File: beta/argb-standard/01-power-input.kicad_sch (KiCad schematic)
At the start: 9 parts, among them J1 SATA_PWR_15P, Q1 AO4407A

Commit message: Audit BETA electrical and pour pipeline
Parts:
- RT1: MPN MF72-5D-20 -> MF72 5D20
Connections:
- net at Q1.1 (S), Q1.2 (S), Q1.3 (S): now also F1.1; no longer J1.7 (Pin_7), J1.8 (Pin_8), J1.9 (Pin_9)
- net at Q1.5 (D), Q1.6 (D), Q1.7 (D)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: now also J1.7 (Pin_7), J1.8 (Pin_8), J1.9 (Pin_9); no longer F1.1
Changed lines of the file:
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@@
 	(symbol
 		(lib_id "cec-vendor:AO4407A")
-		(at 153.67 123.19 270)
-		(unit 1)
-		(exclude_from_sim no)
-		(in_bom yes)
-		(on_board yes)
-		(dnp no)
-		(fields_autoplaced yes)
-		(property "Reference" "Q1" (at 153.67 101.6 90) (effects (font (size 1.27 1.27))))
-		(property "Value" "AO4407A" (at 153.67 130.81 90) (effects (font (size 1.27 1.27))))
+		(at 153.67 123.19 90)
+		(unit 1)
+		(exclude_from_sim no)
+		(in_bom yes)
+		(on_board yes)
+		(dnp no)
+		(fields_autoplaced yes)
+		(property "Reference" "Q1" (at 153.67 106.68 90) (effects (font (size 1.27 1.27))))
+		(property "Value" "AO4407A" (at 153.67 101.6 90) (effects (font (size 1.27 1.27))))
 		(property "Footprint" "cec-Package_SO:SOIC-8_L4.9-W3.9-P1.27-LS6.0-BL" (at 153.67 123.19 0) (effects (font (size 1.27 1.27)) (hide yes)))
-		(property "Datasheet" "" (at 153.67 123.19 0) (effects (font (size 1.27 1.27)) (hide yes)))
+		(property "Datasheet" "https://www.aosmd.com/res/datasheets/AO4407A.pdf" (at 153.67 123.19 0) (effects (font (size 1.27 1.27)) (hide yes)))
 		(property "Manufacturer" "Alpha & Omega Semiconductor" (at 153.67 123.19 0) (effects (font (size 1.27 1.27)) (hide yes)))
 		(property "MPN" "AO4407A" (at 153.67 123.19 0) (effects (font (size 1.27 1.27)) (hide yes)))
@@
 		(property "Value" "2920L700/12MR" (at 185.42 118.36 0) (effects (font (size 1.27 1.27))))
 		(property "Footprint" "cec-Fuse_SMD:F2920" (at 185.42 123.19 0) (effects (font (size 1.27 1.27)) (hide yes)))
-		(property "Datasheet" "" (at 185.42 123.19 0) (effects (font (size 1.27 1.27)) (hide yes)))
+		(property "Datasheet" "https://www.lcsc.com/datasheet/C207092.pdf" (at 185.42 123.19 0) (effects (font (size 1.27 1.27)) (hide yes)))
 		(property "Manufacturer" "Littelfuse" (at 185.42 123.19 0) (effects (font (size 1.27 1.27)) (hide yes)))
 		(property "MPN" "2920L700/12MR" (at 185.42 123.19 0) (effects (font (size 1.27 1.27)) (hide yes)))
@@
 		(property "Value" "MF72-5D-20" (at 210.82 118.36 0) (effects (font (size 1.27 1.27))))
 		(property "Footprint" "cec-Thermistor_THT:RES-TH_L22.0-W7.0-P10.00-D1.0-S2.00" (at 210.82 123.19 0) (effects (font (size 1.27 1.27)) (hide yes)))
-		(property "Datasheet" "" (at 210.82 123.19 0) (effects (font (size 1.27 1.27)) (hide yes)))
+		(property "Datasheet" "https://www.lcsc.com/datasheet/C122780.pdf" (at 210.82 123.19 0) (effects (font (size 1.27 1.27)) (hide yes)))
 		(property "Manufacturer" "Nanjing Shiheng Electronics" (at 210.82 123.19 0) (effects (font (size 1.27 1.27)) (hide yes)))
-		(property "MPN" "MF72-5D-20" (at 210.82 123.19 0) (effects (font (size 1.27 1.27)) (hide yes)))
+		(property "MPN" "MF72 5D20" (at 210.82 123.19 0) (effects (font (size 1.27 1.27)) (hide yes)))
 		(property "LCSC" "C122780" (at 210.82 123.19 0) (effects (font (size 1.27 1.27)) (hide yes)))
 		(property "Description" "Power NTC inrush-current limiter, 5 ohm cold / 7A rated (controlled inrush element -- spec Sec 7.2; OOS at LCSC as of 2026-07-05, flagged, matches this repo's own precedent for a real-but-thin-stock part, cf. the ESP32-S3-MINI-1 pick below)" (at 210.82 123.19 0) (effects (font (size 1.27 1.27)) (hide yes)))
@@
 	(symbol
 		(lib_id "cec-vendor:R_Small")
-		(at 153.67 100.33 0)
-		(unit 1)
-		(exclude_from_sim no)
-		(in_bom yes)
-		(on_board yes)
-		(dnp no)
-		(fields_autoplaced yes)
-		(property "Reference" "R1" (at 155.702 99.06 0) (effects (font (size 1.27 1.27)) (justify left)))
-		(property "Value" "10kΩ" (at 155.702 101.6 0) (effects (font (size 1.27 1.27)) (justify left)))
-		(property "Footprint" "cec-Resistor_SMD:R_0402_1005Metric" (at 153.67 100.33 0) (effects (font (size 1.27 1.27)) (hide yes)))
-		(property "Datasheet" "" (at 153.67 100.33 0) (effects (font (size 1.27 1.27)) (hide yes)))
-		(property "Manufacturer" "UNI-ROYAL" (at 153.67 100.33 0) (effects (font (size 1.27 1.27)) (hide yes)))
-		(property "MPN" "0402WGF1002TCE" (at 153.67 100.33 0) (effects (font (size 1.27 1.27)) (hide yes)))
-		(property "LCSC" "C25744" (at 153.67 100.33 0) (effects (font (size 1.27 1.27)) (hide yes)))
+		(at 153.67 115.57 0)
+		(unit 1)
+		(exclude_from_sim no)
+		(in_bom yes)
+		(on_board yes)
+		(dnp no)
+		(fields_autoplaced yes)
+		(property "Reference" "R1" (at 156.972 114.3 0) (effects (font (size 1.27 1.27)) (justify left)))
+		(property "Value" "10kΩ" (at 155.702 116.84 0) (effects (font (size 1.27 1.27)) (justify left)))
+		(property "Footprint" "cec-Resistor_SMD:R_0402_1005Metric" (at 153.67 115.57 0) (effects (font (size 1.27 1.27)) (hide yes)))
+		(property "Datasheet" "" (at 153.67 115.57 0) (effects (font (size 1.27 1.27)) (hide yes)))
+		(property "Manufacturer" "UNI-ROYAL" (at 153.67 115.57 0) (effects (font (size 1.27 1.27)) (hide yes)))
+		(property "MPN" "0402WGF1002TCE" (at 153.67 115.57 0) (effects (font (size 1.27 1.27)) (hide yes)))
+		(property "LCSC" "C25744" (at 153.67 115.57 0) (effects (font (size 1.27 1.27)) (hide yes)))
 		(pin "1")
 		(pin "2")
@@
 	(wire (pts (xy 135.89 123.19) (xy 146.05 123.19))
 		(stroke (width 0) (type default)))
+	(wire (pts (xy 135.89 120.65) (xy 146.05 120.65))
+		(stroke (width 0) (type default)))
+	(wire (pts (xy 135.89 125.73) (xy 146.05 125.73))
+		(stroke (width 0) (type default)))
+	(wire (pts (xy 135.89 118.11) (xy 146.05 118.11))
+		(stroke (width 0) (type default)))
+	(wire (pts (xy 135.89 118.11) (xy 135.89 120.65))
+		(stroke (width 0) (type default)))
+	(wire (pts (xy 135.89 120.65) (xy 135.89 123.19))
+		(stroke (width 0) (type default)))
 	(wire (pts (xy 135.89 123.19) (xy 135.89 125.73))
 		(stroke (width 0) (type default)))
-	(wire (pts (xy 135.89 125.73) (xy 146.05 125.73))
-		(stroke (width 0) (type default)))
-	(wire (pts (xy 135.89 123.19) (xy 135.89 120.65))
-		(stroke (width 0) (type default)))
-	(wire (pts (xy 135.89 120.65) (xy 146.05 120.65))
-		(stroke (width 0) (type default)))
 	(wire (pts (xy 161.29 123.19) (xy 171.45 123.19))
 		(stroke (width 0) (type default)))
+	(wire (pts (xy 161.29 120.65) (xy 171.45 120.65))
+		(stroke (width 0) (type default)))
 	(wire (pts (xy 161.29 125.73) (xy 171.45 125.73))
 		(stroke (width 0) (type default)))
-	(wire (pts (xy 161.29 120.65) (xy 171.45 120.65))
-		(stroke (width 0) (type default)))
-	(wire (pts (xy 161.29 128.27) (xy 171.45 128.27))
-		(stroke (width 0) (type default)))
-	(wire (pts (xy 171.45 120.65) (xy 171.45 128.27))
-		(stroke (width 0) (type default)))
-	(wire (pts (xy 153.67 115.57) (xy 153.67 102.87))
-		(stroke (width 0) (type default)))
-	(wire (pts (xy 171.45 125.73) (xy 171.45 123.19))
+	(wire (pts (xy 153.67 130.81) (xy 153.67 118.11))
 		(stroke (width 0) (type default)))
 	(wire (pts (xy 171.45 123.19) (xy 180.34 123.19))
 		(stroke (width 0) (type default)))
+	(wire (pts (xy 171.45 120.65) (xy 171.45 123.19))
+		(stroke (width 0) (type default)))
+	(wire (pts (xy 171.45 123.19) (xy 171.45 125.73))
+		(stroke (width 0) (type default)))
 	(wire (pts (xy 190.5 123.19) (xy 205.74 123.19))
 		(stroke (width 0) (type default)))
@@
 	(wire (pts (xy 110.49 133.35) (xy 104.14 133.35))
 		(stroke (width 0) (type default)))
-	(wire (pts (xy 153.67 97.79) (xy 153.67 93.98))
+	(wire (pts (xy 153.67 113.03) (xy 153.67 109.22))
 		(stroke (width 0) (type default)))
 	(wire (pts (xy 226.06 151.13) (xy 226.06 154.94))
@@
 		(stroke (width 0) (type default)))
 	(junction (at 97.79 123.19) (diameter 0) (color 0 0 0 0))
+	(junction (at 135.89 120.65) (diameter 0) (color 0 0 0 0))
 	(junction (at 135.89 123.19) (diameter 0) (color 0 0 0 0))
 	(junction (at 171.45 123.19) (diameter 0) (color 0 0 0 0))
@@
 	(symbol
 		(lib_id "cec-power:GND")
-		(at 153.67 93.98 180)
-		(unit 1)
-		(exclude_from_sim no)
-		(in_bom yes)
-		(on_board yes)
-		(dnp no)
-		(property "Reference" "#PWR107" (at 153.67 91.44 0) (effects (font (size 1.27 1.27)) (hide yes)))
-		(property "Value" "GND" (at 153.67 88.9 0) (effects (font (size 1.27 1.27))))
-		(pin "1")
-		(instances
+		(at 153.67 109.22 180)
+		(unit 1)
+		(exclude_from_sim no)
+		(in_bom yes)
+		(on_board yes)
+		(dnp no)
+		(property "Reference" "#PWR107" (at 153.67 106.68 0) (effects (font (size 1.27 1.27)) (hide yes)))
+		(property "Value" "GND" (at 153.67 104.14 0) (effects (font (size 1.27 1.27))))
+		(pin "1")
+		(instances

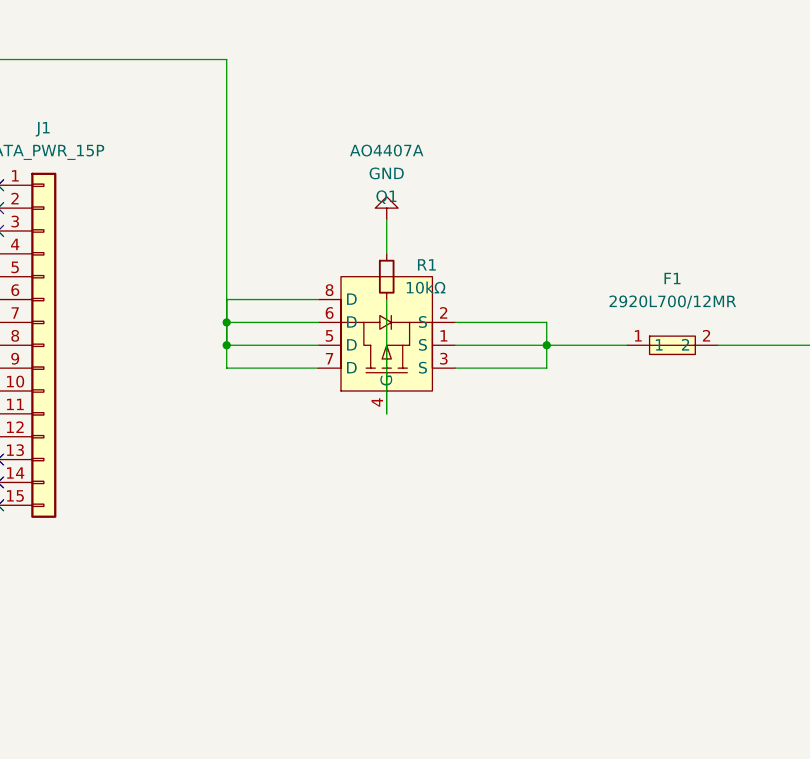
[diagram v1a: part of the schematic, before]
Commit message: Audit BETA power designs and harden PCB pipeline
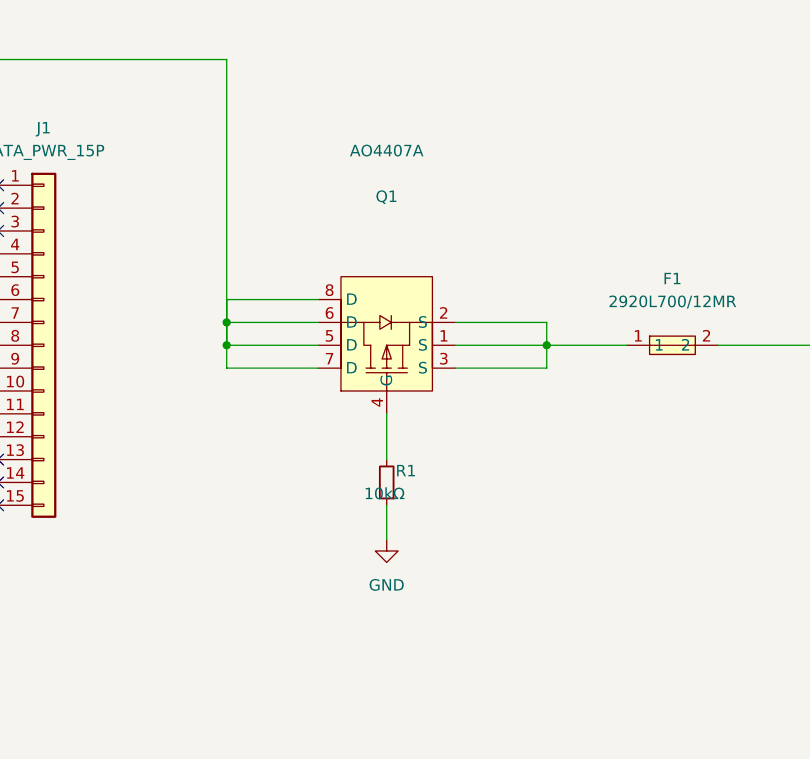
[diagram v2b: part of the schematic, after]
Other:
- moved on the sheet: R1
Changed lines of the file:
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@@
 	(symbol
 		(lib_id "cec-vendor:R_Small")
-		(at 153.67 115.57 0)
-		(unit 1)
-		(exclude_from_sim no)
-		(in_bom yes)
-		(on_board yes)
-		(dnp no)
-		(fields_autoplaced yes)
-		(property "Reference" "R1" (at 156.972 114.3 0) (effects (font (size 1.27 1.27)) (justify left)))
-		(property "Value" "10kΩ" (at 155.702 116.84 0) (effects (font (size 1.27 1.27)) (justify left)))
-		(property "Footprint" "cec-Resistor_SMD:R_0402_1005Metric" (at 153.67 115.57 0) (effects (font (size 1.27 1.27)) (hide yes)))
-		(property "Datasheet" "" (at 153.67 115.57 0) (effects (font (size 1.27 1.27)) (hide yes)))
-		(property "Manufacturer" "UNI-ROYAL" (at 153.67 115.57 0) (effects (font (size 1.27 1.27)) (hide yes)))
-		(property "MPN" "0402WGF1002TCE" (at 153.67 115.57 0) (effects (font (size 1.27 1.27)) (hide yes)))
-		(property "LCSC" "C25744" (at 153.67 115.57 0) (effects (font (size 1.27 1.27)) (hide yes)))
+		(at 153.67 138.43 180)
+		(unit 1)
+		(exclude_from_sim no)
+		(in_bom yes)
+		(on_board yes)
+		(dnp no)
+		(fields_autoplaced yes)
+		(property "Reference" "R1" (at 156.972 137.16 0) (effects (font (size 1.27 1.27)) (justify left)))
+		(property "Value" "10kΩ" (at 155.702 139.7 0) (effects (font (size 1.27 1.27)) (justify left)))
+		(property "Footprint" "cec-Resistor_SMD:R_0402_1005Metric" (at 153.67 138.43 0) (effects (font (size 1.27 1.27)) (hide yes)))
+		(property "Datasheet" "" (at 153.67 138.43 0) (effects (font (size 1.27 1.27)) (hide yes)))
+		(property "Manufacturer" "UNI-ROYAL" (at 153.67 138.43 0) (effects (font (size 1.27 1.27)) (hide yes)))
+		(property "MPN" "0402WGF1002TCE" (at 153.67 138.43 0) (effects (font (size 1.27 1.27)) (hide yes)))
+		(property "LCSC" "C25744" (at 153.67 138.43 0) (effects (font (size 1.27 1.27)) (hide yes)))
 		(pin "1")
 		(pin "2")
@@
 	(wire (pts (xy 161.29 125.73) (xy 171.45 125.73))
 		(stroke (width 0) (type default)))
-	(wire (pts (xy 153.67 130.81) (xy 153.67 118.11))
+	(wire (pts (xy 153.67 130.81) (xy 153.67 135.89))
 		(stroke (width 0) (type default)))
 	(wire (pts (xy 171.45 123.19) (xy 180.34 123.19))
@@
 	(wire (pts (xy 110.49 133.35) (xy 104.14 133.35))
 		(stroke (width 0) (type default)))
-	(wire (pts (xy 153.67 113.03) (xy 153.67 109.22))
+	(wire (pts (xy 153.67 140.97) (xy 153.67 144.78))
 		(stroke (width 0) (type default)))
 	(wire (pts (xy 226.06 151.13) (xy 226.06 154.94))
@@
 	(symbol
 		(lib_id "cec-power:GND")
-		(at 153.67 109.22 180)
-		(unit 1)
-		(exclude_from_sim no)
-		(in_bom yes)
-		(on_board yes)
-		(dnp no)
-		(property "Reference" "#PWR107" (at 153.67 106.68 0) (effects (font (size 1.27 1.27)) (hide yes)))
-		(property "Value" "GND" (at 153.67 104.14 0) (effects (font (size 1.27 1.27))))
-		(pin "1")
-		(instances
+		(at 153.67 144.78 0)
+		(unit 1)
+		(exclude_from_sim no)
+		(in_bom yes)
+		(on_board yes)
+		(dnp no)
+		(property "Reference" "#PWR107" (at 153.67 142.24 0) (effects (font (size 1.27 1.27)) (hide yes)))
+		(property "Value" "GND" (at 153.67 149.86 0) (effects (font (size 1.27 1.27))))
+		(pin "1")
+		(instances
